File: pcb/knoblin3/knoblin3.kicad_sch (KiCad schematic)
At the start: 9 parts, among them J1 Conn_01x04_Male, J2 Conn_01x04_Female, SW1 RotaryEncoder_Switch, SW2 RotaryEncoder_Switch, SW3 RotaryEncoder_Switch, SW4 SW_SPST, SW5 SW_SPST, SW6 SW_SPST, U1 SeeeduinoXIAO

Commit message: add new files
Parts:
- added H1: (no value), symbol Mechanical:MountingHole
- added H2: MountingHole, symbol Mechanical:MountingHole
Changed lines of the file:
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@@
+    )
+  )
+  (symbol (lib_id "Mechanical:MountingHole") (at 158.75 92.71 0) (unit 1)
+    (in_bom yes) (on_board yes) (fields_autoplaced)
+    (property "Reference" "H2" (id 0) (at 161.29 91.8753 0)
+      (effects (font (size 1.27 1.27)) (justify left))
+    )
+    (property "Value" "MountingHole" (id 1) (at 161.29 94.4122 0)
+      (effects (font (size 1.27 1.27)) (justify left))
+    )
+    (property "Footprint" "" (id 2) (at 158.75 92.71 0)
+      (effects (font (size 1.27 1.27)) hide)
+    )
+    (property "Datasheet" "~" (id 3) (at 158.75 92.71 0)
+      (effects (font (size 1.27 1.27)) hide)
     )
   )
@@
     (pin "2")
   )
+  (symbol (lib_id "Mechanical:MountingHole") (at 153.67 92.71 0) (unit 1)
+    (in_bom yes) (on_board yes) (fields_autoplaced)
+    (property "Reference" "H1" (id 0) (at 156.21 91.8753 0)
+      (effects (font (size 1.27 1.27)) (justify left))
+    )
+    (property "Value" "" (id 1) (at 156.21 94.4122 0)
+      (effects (font (size 1.27 1.27)) (justify left))
+    )
+    (property "Footprint" "" (id 2) (at 153.67 92.71 0)
+      (effects (font (size 1.27 1.27)) hide)
+    )
+    (property "Datasheet" "~" (id 3) (at 153.67 92.71 0)
+      (effects (font (size 1.27 1.27)) hide)
+    )
+  )
   (sheet_instances
     (path "/" (page "1"))
   )
   (symbol_instances
+    (path "/db293caa-a836-4ccc-80a9-5f4edb0c654b"
+      (reference "H1") (unit 1) (value "MountingHole") (footprint "MountingHole:MountingHole_2.2mm_M2_DIN965")
+    )
+    (path "/098ab8c1-1380-40a5-b8a8-396b8356b7d7"
+      (reference "H2") (unit 1) (value "MountingHole") (footprint "MountingHole:MountingHole_2.2mm_M2_DIN965")
+    )
     (path "/921e5b26-291f-45fe-95b0-cf97f723c679"
       (reference "J1") (unit 1) (value "Conn_01x04_Male") (footprint "Connector_PinSocket_2.54mm:PinSocket_1x04_P2.54mm_Vertical")

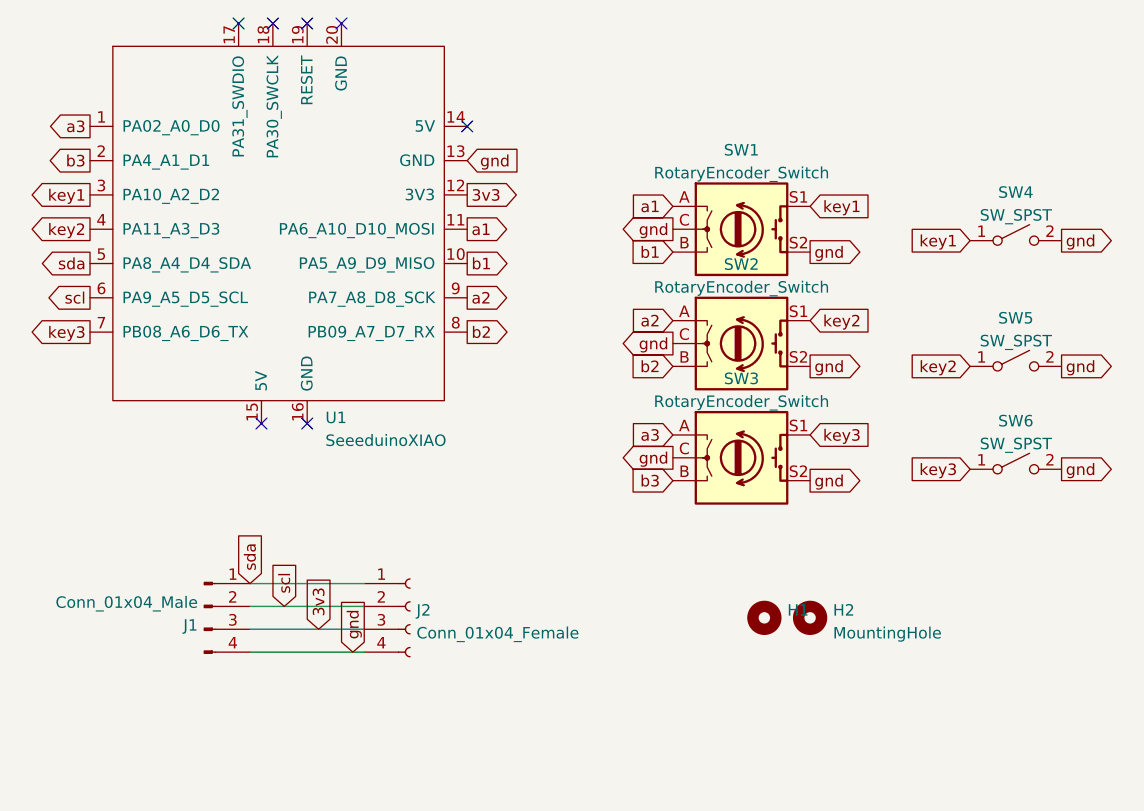
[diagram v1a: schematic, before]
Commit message: update knoblin to v2.0
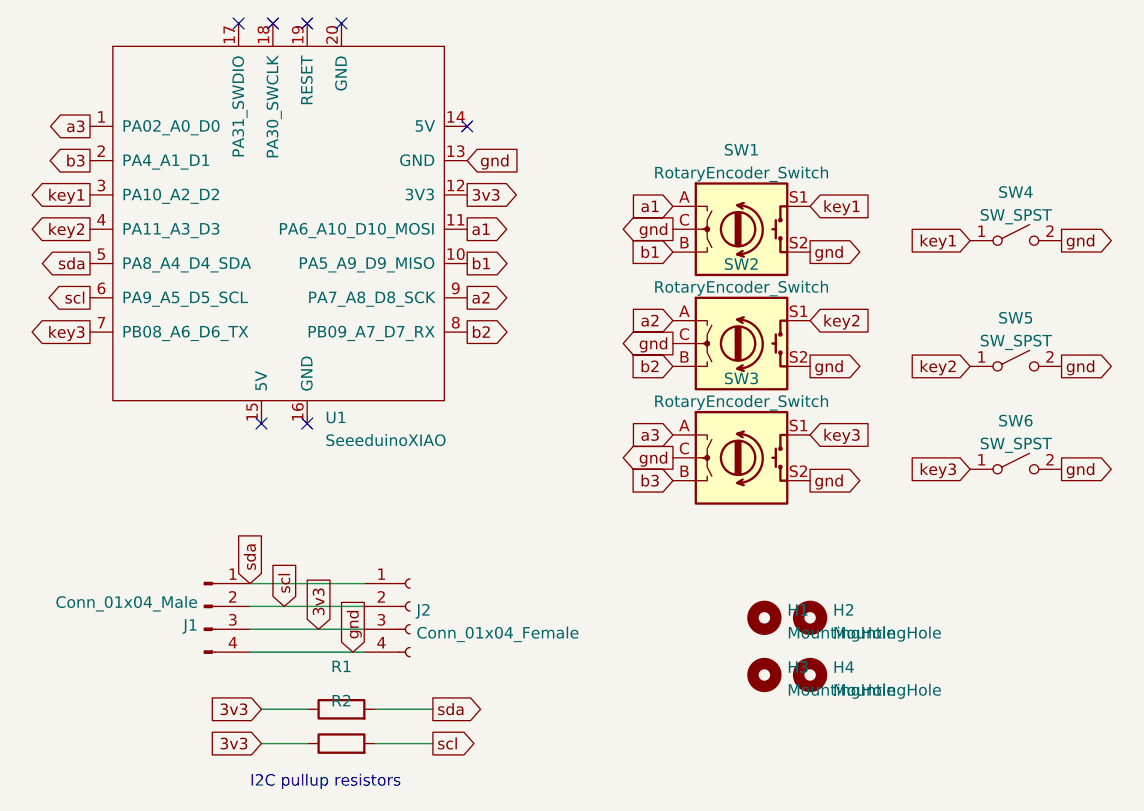
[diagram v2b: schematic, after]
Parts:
- added H3, H4: MountingHole, MountingHole:MountingHole_2.2mm_M2_DIN965, symbol Mechanical:MountingHole
- added R1, R2: (no value), symbol Device:R
- H1: value (none) -> MountingHole; footprint (none) -> MountingHole:MountingHole_2.2mm_M2_DIN965
- H2: footprint (none) -> MountingHole:MountingHole_2.2mm_M2_DIN965
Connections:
- net 3v3: now also R1.1, R2.1
- net scl: now also R2.2
- net sda: now also R1.2
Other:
- note added: "I2C pullup resistors"
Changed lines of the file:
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@@
+    (stroke (width 0) (type default) (color 0 0 0 0))
+  )
+  (wire (pts (xy 97.79 102.87) (xy 102.87 102.87))
+    (stroke (width 0) (type default) (color 0 0 0 0))
+  )
+  (wire (pts (xy 110.49 106.68) (xy 116.84 106.68))
     (stroke (width 0) (type default) (color 0 0 0 0))
   )
@@
     (stroke (width 0) (type default) (color 0 0 0 0))
   )
+  (wire (pts (xy 97.79 106.68) (xy 102.87 106.68))
+    (stroke (width 0) (type default) (color 0 0 0 0))
+  )
   (wire (pts (xy 96.52 93.98) (xy 109.22 93.98))
     (stroke (width 0) (type default) (color 0 0 0 0))
   )
+  (wire (pts (xy 110.49 102.87) (xy 116.84 102.87))
+    (stroke (width 0) (type default) (color 0 0 0 0))
+  )
+  (text "I2C pullup resistors" (at 96.52 111.76 0)
+    (effects (font (size 1.27 1.27)) (justify left bottom))
+  )
   (global_label "gnd" (shape input) (at 120.65 41.91 0) (fields_autoplaced)
     (effects (font (size 1.27 1.27)) (justify left))
@@
     )
   )
+  (global_label "3v3" (shape input) (at 97.79 102.87 180) (fields_autoplaced)
+    (effects (font (size 1.27 1.27)) (justify right))
+    (property "Intersheet References" "${INTERSHEET_REFS}" (id 0) (at 91.9902 102.7906 0)
+      (effects (font (size 1.27 1.27)) (justify right) hide)
+    )
+  )
   (global_label "key1" (shape input) (at 176.53 50.8 180) (fields_autoplaced)
     (effects (font (size 1.27 1.27)) (justify right))
@@
     )
   )
+  (global_label "scl" (shape output) (at 116.84 106.68 0) (fields_autoplaced)
+    (effects (font (size 1.27 1.27)) (justify left))
+    (property "Intersheet References" "${INTERSHEET_REFS}" (id 0) (at 122.035 106.6006 0)
+      (effects (font (size 1.27 1.27)) (justify left) hide)
+    )
+  )
   (global_label "a1" (shape output) (at 120.65 49.53 0) (fields_autoplaced)
     (effects (font (size 1.27 1.27)) (justify left))
@@
     )
   )
+  (global_label "sda" (shape output) (at 116.84 102.87 0) (fields_autoplaced)
+    (effects (font (size 1.27 1.27)) (justify left))
+    (property "Intersheet References" "${INTERSHEET_REFS}" (id 0) (at 122.5793 102.7906 0)
+      (effects (font (size 1.27 1.27)) (justify left) hide)
+    )
+  )
   (global_label "gnd" (shape input) (at 107.95 96.52 90) (fields_autoplaced)
     (effects (font (size 1.27 1.27)) (justify left))
@@
     )
   )
+  (global_label "3v3" (shape input) (at 97.79 106.68 180) (fields_autoplaced)
+    (effects (font (size 1.27 1.27)) (justify right))
+    (property "Intersheet References" "${INTERSHEET_REFS}" (id 0) (at 91.9902 106.6006 0)
+      (effects (font (size 1.27 1.27)) (justify right) hide)
+    )
+  )
   (global_label "b3" (shape input) (at 143.51 77.47 180) (fields_autoplaced)
     (effects (font (size 1.27 1.27)) (justify right))
@@
     )
   )
+  (symbol (lib_id "Device:R") (at 106.68 106.68 90) (unit 1)
+    (in_bom yes) (on_board yes) (fields_autoplaced)
+    (property "Reference" "R2" (id 0) (at 106.68 101.9642 90))
+    (property "Value" "" (id 1) (at 106.68 104.5011 90))
+    (property "Footprint" "" (id 2) (at 106.68 108.458 90)
+      (effects (font (size 1.27 1.27)) hide)
+    )
+    (property "Datasheet" "~" (id 3) (at 106.68 106.68 0)
+      (effects (font (size 1.27 1.27)) hide)
+    )
+    (pin "1")
+    (pin "2")
+  )
   (symbol (lib_id "Mechanical:MountingHole") (at 158.75 92.71 0) (unit 1)
     (in_bom yes) (on_board yes) (fields_autoplaced)
@@
       (effects (font (size 1.27 1.27)) (justify left))
     )
-    (property "Footprint" "" (id 2) (at 158.75 92.71 0)
+    (property "Footprint" "MountingHole:MountingHole_2.2mm_M2_DIN965" (id 2) (at 158.75 92.71 0)
       (effects (font (size 1.27 1.27)) hide)
     )
     (property "Datasheet" "~" (id 3) (at 158.75 92.71 0)
+      (effects (font (size 1.27 1.27)) hide)
+    )
+  )
+  (symbol (lib_id "Mechanical:MountingHole") (at 153.67 99.06 0) (unit 1)
+    (in_bom yes) (on_board yes) (fields_autoplaced)
+    (property "Reference" "H3" (id 0) (at 156.21 98.2253 0)
+      (effects (font (size 1.27 1.27)) (justify left))
+    )
+    (property "Value" "MountingHole" (id 1) (at 156.21 100.7622 0)
+      (effects (font (size 1.27 1.27)) (justify left))
+    )
+    (property "Footprint" "MountingHole:MountingHole_2.2mm_M2_DIN965" (id 2) (at 153.67 99.06 0)
+      (effects (font (size 1.27 1.27)) hide)
+    )
+    (property "Datasheet" "~" (id 3) (at 153.67 99.06 0)
       (effects (font (size 1.27 1.27)) hide)
     )
@@
     (pin "9")
   )
+  (symbol (lib_id "Device:R") (at 106.68 102.87 90) (unit 1)
+    (in_bom yes) (on_board yes) (fields_autoplaced)
+    (property "Reference" "R1" (id 0) (at 106.68 98.1542 90))
+    (property "Value" "" (id 1) (at 106.68 100.6911 90))
+    (property "Footprint" "" (id 2) (at 106.68 104.648 90)
+      (effects (font (size 1.27 1.27)) hide)
+    )
+    (property "Datasheet" "~" (id 3) (at 106.68 102.87 0)
+      (effects (font (size 1.27 1.27)) hide)
+    )
+    (pin "1")
+    (pin "2")
+  )
   (symbol (lib_id "Switch:SW_SPST") (at 181.61 50.8 0) (unit 1)
     (in_bom yes) (on_board yes) (fields_autoplaced)
@@
     (pin "4")
   )
+  (symbol (lib_id "Mechanical:MountingHole") (at 158.75 99.06 0) (unit 1)
+    (in_bom yes) (on_board yes) (fields_autoplaced)
+    (property "Reference" "H4" (id 0) (at 161.29 98.2253 0)
+      (effects (font (size 1.27 1.27)) (justify left))
+    )
+    (property "Value" "MountingHole" (id 1) (at 161.29 100.7622 0)
+      (effects (font (size 1.27 1.27)) (justify left))
+    )
+    (property "Footprint" "MountingHole:MountingHole_2.2mm_M2_DIN965" (id 2) (at 158.75 99.06 0)
+      (effects (font (size 1.27 1.27)) hide)
+    )
+    (property "Datasheet" "~" (id 3) (at 158.75 99.06 0)
+      (effects (font (size 1.27 1.27)) hide)
+    )
+  )
   (symbol (lib_id "Connector:Conn_01x04_Female") (at 114.3 91.44 0) (unit 1)
     (in_bom yes) (on_board yes) (fields_autoplaced)
@@
       (effects (font (size 1.27 1.27)) (justify left))
     )
-    (property "Value" "" (id 1) (at 156.21 94.4122 0)
-      (effects (font (size 1.27 1.27)) (justify left))
-    )
-    (property "Footprint" "" (id 2) (at 153.67 92.71 0)
+    (property "Value" "MountingHole" (id 1) (at 156.21 94.4122 0)
+      (effects (font (size 1.27 1.27)) (justify left))
+    )
+    (property "Footprint" "MountingHole:MountingHole_2.2mm_M2_DIN965" (id 2) (at 153.67 92.71 0)
       (effects (font (size 1.27 1.27)) hide)
     )
@@
       (reference "H2") (unit 1) (value "MountingHole") (footprint "MountingHole:MountingHole_2.2mm_M2_DIN965")
     )
+    (path "/15ddbae8-4879-44da-8c42-497366b84781"
+      (reference "H3") (unit 1) (value "MountingHole") (footprint "MountingHole:MountingHole_2.2mm_M2_DIN965")
+    )
+    (path "/a54a2d51-4b66-4d14-b33d-1444b55de06d"
+      (reference "H4") (unit 1) (value "MountingHole") (footprint "MountingHole:MountingHole_2.2mm_M2_DIN965")
+    )
     (path "/921e5b26-291f-45fe-95b0-cf97f723c679"
       (reference "J1") (unit 1) (value "Conn_01x04_Male") (footprint "Connector_PinSocket_2.54mm:PinSocket_1x04_P2.54mm_Vertical")
@@
       (reference "J2") (unit 1) (value "Conn_01x04_Female") (footprint "Connector_PinSocket_2.54mm:PinSocket_1x04_P2.54mm_Vertical")
     )
+    (path "/5496fd8b-7b7f-469c-96a4-74dadaa08803"
+      (reference "R1") (unit 1) (value "R") (footprint "Resistor_SMD:R_1206_3216Metric_Pad1.30x1.75mm_HandSolder")
+    )
+    (path "/03fafb79-e9b4-46d8-a707-df52bba50ac0"
+      (reference "R2") (unit 1) (value "R") (footprint "Resistor_SMD:R_1206_3216Metric_Pad1.30x1.75mm_HandSolder")
+    )
     (path "/6f99616a-ac0d-4a8d-b9bb-5c1c2e4f0bc9"
